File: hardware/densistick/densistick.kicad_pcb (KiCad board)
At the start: 4 copper layers, 85 x 22 mm, 67 parts, among them J1 Cable, SW1 SW_Push, U1 TSL2585, U2 USBLC6-2SC6, U3 MIC4812, U4 FT260Q, U5 MIC5365-1.8YC5, U6 CAT24C08, U7 MCP4017-104E/LT

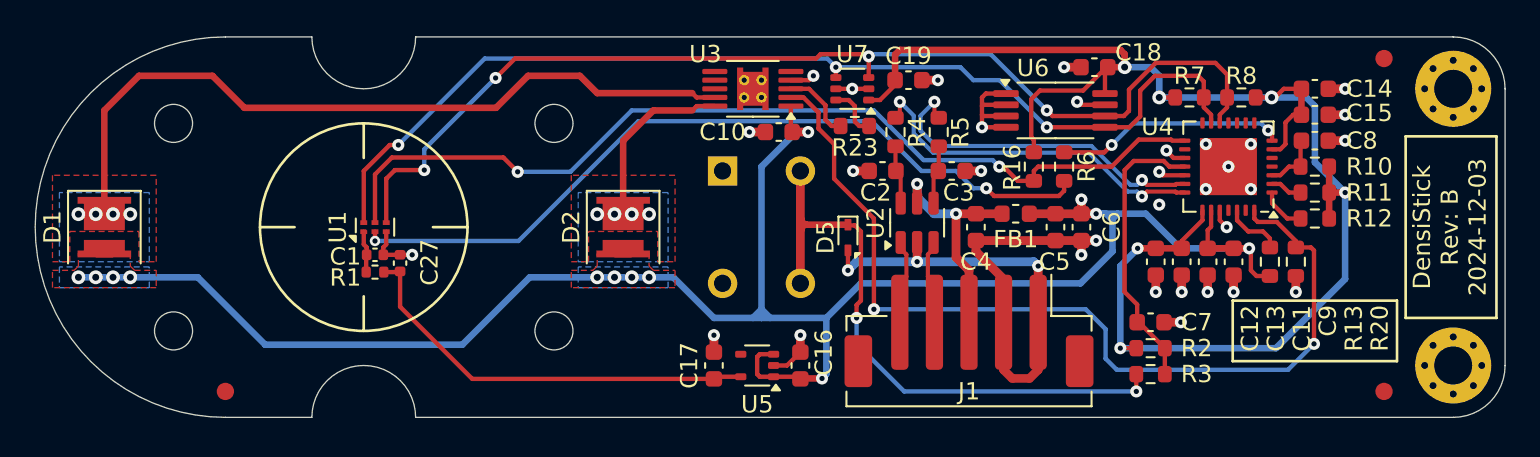
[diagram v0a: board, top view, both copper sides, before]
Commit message: Change light sensor on peripherals
Ref #85
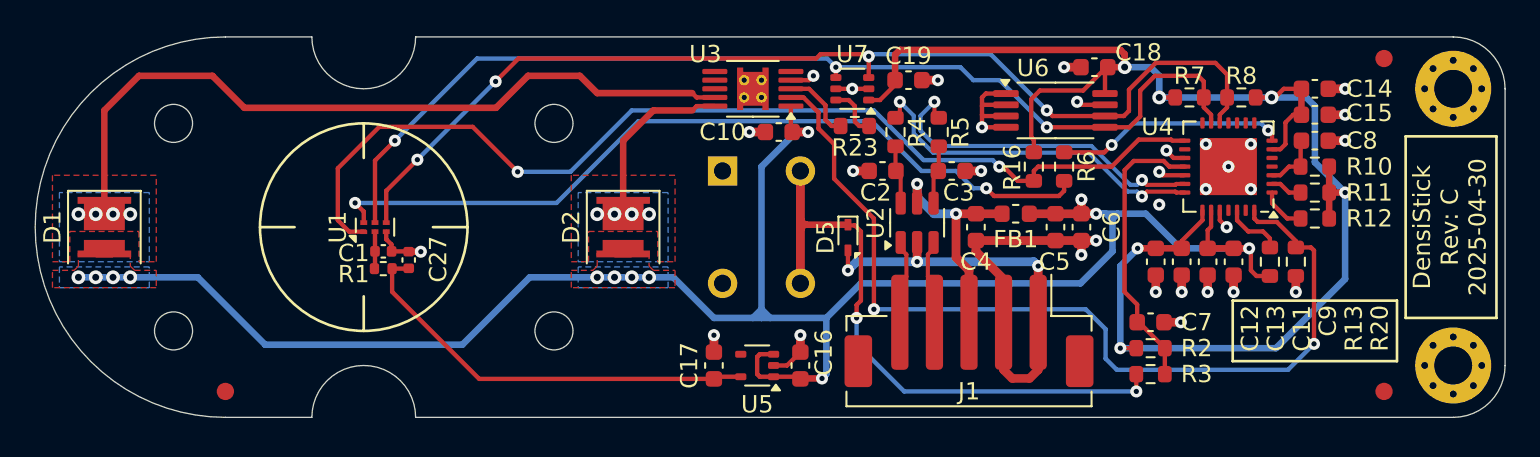
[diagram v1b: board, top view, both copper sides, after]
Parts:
- moved C27 0.53 mm to (62.6, 69.9)
- moved C1 0.52 mm to (61.1, 69.4)
- moved R1 0.52 mm to (61.1, 70.4)
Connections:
- U1 pad 1: Net-(U1-VDD) -> /TSL_INT
- U1 pad 2: /TSL_VSYNC -> Net-(U1-VDD)
- U1 pad 5: /TSL_INT -> /I2C_SDA
- U1 pad 6: /I2C_SDA -> /TSL_VSYNC
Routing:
- net /TSL_INT: track 54.9 -> 60.3 mm
- net /I2C_SCL: track 62.9 -> 61.8 mm
- net /TSL_VSYNC: track 45.8 -> 46.8 mm

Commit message: Fix component value and some symbol/footprint updates
Forgot to change the "Value" field of the light sensor when switching it
from the TSL2585 to the TSL2522.

Also pulled in some minor KiCad changes to symbols and footprints, all
of which affect metadata and do not change the board layout itself.
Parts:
- U1: value TSL2585 -> TSL2522

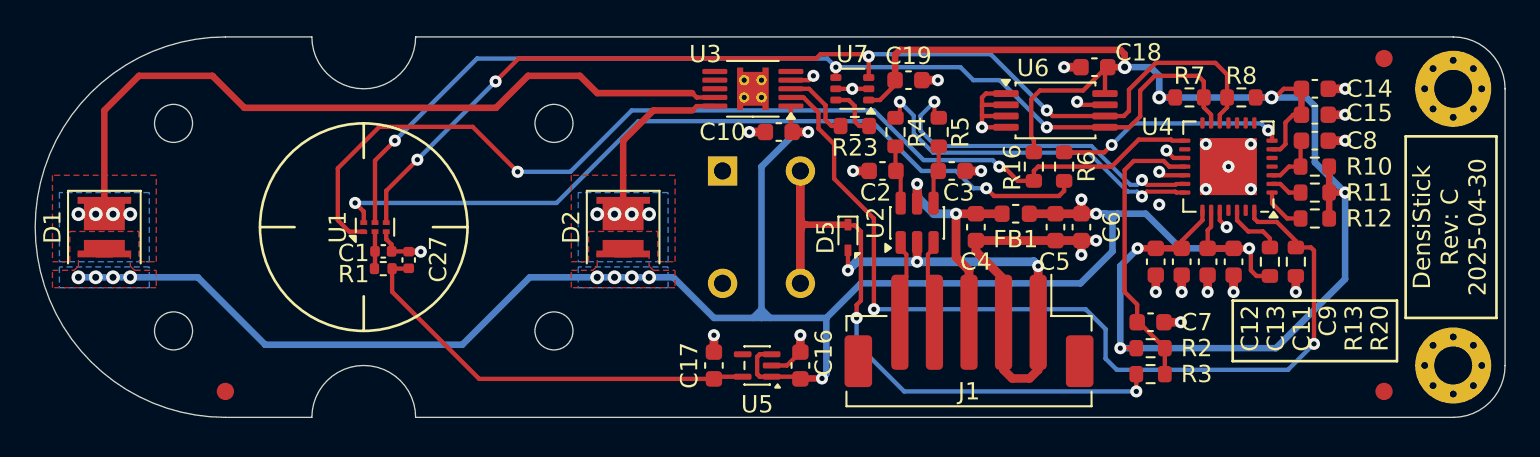
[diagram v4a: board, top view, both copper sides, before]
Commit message: Update DensiStick fiducial and position data
Add a fourth fiducial
Adjust some component silkscreen locations for more fiducial clearance
Tweak fiducial locations
Update metadata for position file exclusion
Update board date, but not revision
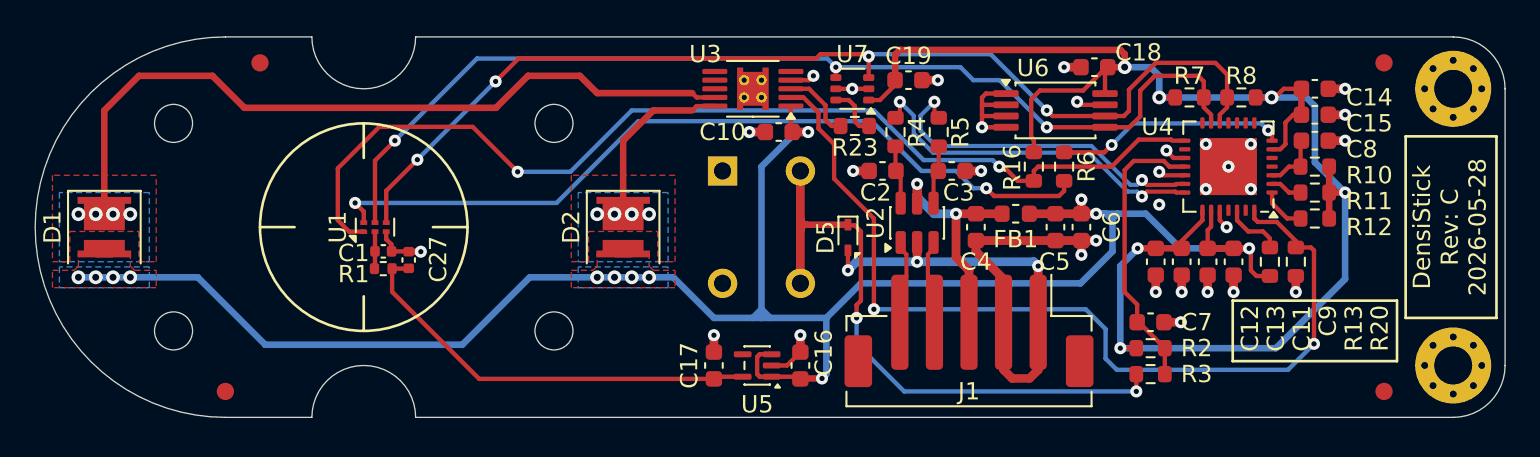
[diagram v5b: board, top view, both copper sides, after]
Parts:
- added FID4: Fiducial, Fiducial:Fiducial_1mm_Mask2mm, F.Cu at (54.0, 58.5)
- moved FID3 0.25 mm to (119.0, 58.5)
